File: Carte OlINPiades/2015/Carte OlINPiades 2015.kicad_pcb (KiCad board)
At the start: 2 copper layers, 283 parts, among them U1 dsPIC33FJ128MC802, U2 LM7805, U3 LM2937-3.3

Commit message: retourne leds
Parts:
- moved D1 1.00 mm to (47.5, 64.0), turned to 180 degrees
- moved D10 1.00 mm to (106.0, 64.0), turned to 180 degrees
- moved D100 1.00 mm to (67.0, 103.0), turned to 180 degrees
- moved D101 1.00 mm to (73.5, 103.0), turned to 180 degrees
- moved D102 1.00 mm to (80.0, 103.0), turned to 180 degrees
- moved D103 1.00 mm to (86.5, 103.0), turned to 180 degrees
- moved D104 1.00 mm to (93.0, 103.0), turned to 180 degrees
- moved D105 1.00 mm to (99.5, 103.0), turned to 180 degrees
- moved D106 1.00 mm to (106.0, 103.0), turned to 180 degrees
- moved D107 1.00 mm to (112.5, 103.0), turned to 180 degrees
- moved D108 1.00 mm to (119.0, 103.0), turned to 180 degrees
- moved D109 1.00 mm to (125.5, 103.0), turned to 180 degrees
- moved D11 1.00 mm to (112.5, 64.0), turned to 180 degrees
- moved D110 1.00 mm to (132.0, 103.0), turned to 180 degrees
- moved D111 1.00 mm to (138.5, 103.0), turned to 180 degrees
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
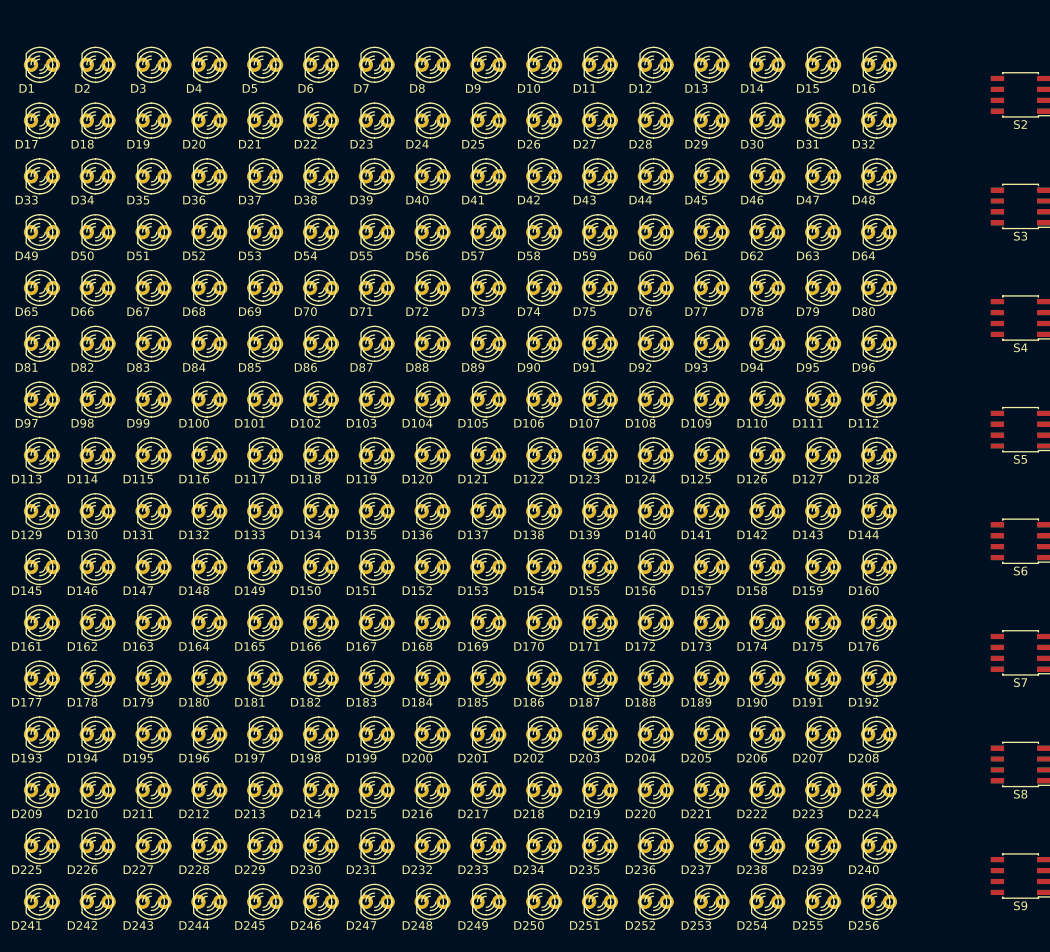
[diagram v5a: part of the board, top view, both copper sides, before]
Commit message: ajoute une face de piste de led
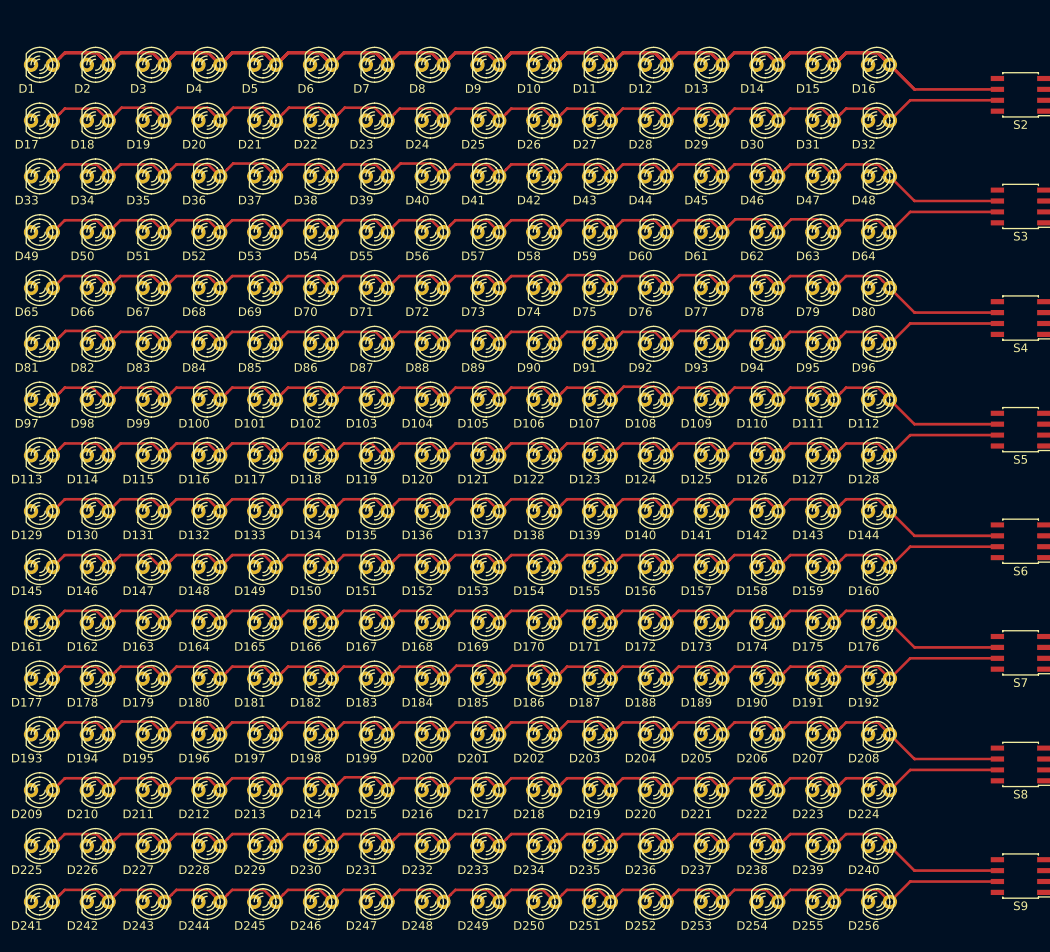
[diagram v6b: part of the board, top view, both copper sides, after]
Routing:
- net Net-(D1-Pad1): track 0.00 -> 477.0 mm
- net Net-(D17-Pad1): track 0.00 -> 128.8 mm
- net Net-(D65-Pad1): track 0.00 -> 128.7 mm
- net Net-(D193-Pad1): track 0.00 -> 128.7 mm
- net Net-(D33-Pad1): track 0.00 -> 128.7 mm
- net Net-(D81-Pad1): track 0.00 -> 128.7 mm
- net Net-(D100-Pad1): track 0.00 -> 128.6 mm
- net Net-(D225-Pad1): track 0.00 -> 128.5 mm
- net Net-(D161-Pad1): track 0.00 -> 128.5 mm
- net Net-(D129-Pad1): track 0.00 -> 128.5 mm
- net Net-(D49-Pad1): track 0.00 -> 128.5 mm
- net Net-(D177-Pad1): track 0.00 -> 128.5 mm
- net Net-(D209-Pad1): track 0.00 -> 128.4 mm
- net Net-(D241-Pad1): track 0.00 -> 128.3 mm
- net Net-(D145-Pad1): track 0.00 -> 128.3 mm
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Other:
- net class Pisa added: clearance 0.4, trace_width 0.308, via_dia 0.8, via_drill 0.6

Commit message: ajoute l'autre face de piste de leds
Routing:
- net Net-(D115-Pad2): track 0.00 -> 97.5 mm
- net Net-(D114-Pad2): track 0.00 -> 97.5 mm
- net Net-(D112-Pad2): track 0.00 -> 97.5 mm
- net Net-(D111-Pad2): track 0.00 -> 97.5 mm
- net Net-(D110-Pad2): track 0.00 -> 97.5 mm
- net Net-(D109-Pad2): track 0.00 -> 97.5 mm
- net Net-(D108-Pad2): track 0.00 -> 97.5 mm
- net Net-(D107-Pad2): track 0.00 -> 97.5 mm
- net Net-(D105-Pad2): track 0.00 -> 97.5 mm
- net Net-(D104-Pad2): track 0.00 -> 97.5 mm
- net Net-(D103-Pad2): track 0.00 -> 97.5 mm
- net Net-(D102-Pad2): track 0.00 -> 97.5 mm
- net Net-(D101-Pad2): track 0.00 -> 97.5 mm
- net Net-(D100-Pad2): track 0.00 -> 97.5 mm
- net Net-(D10-Pad2): track 0.00 -> 97.5 mm
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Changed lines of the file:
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@@
     (thickness 1.6)
     (drawings 0)
-    (tracks 1174)
+    (tracks 1191)
     (zones 0)
     (modules 283)
@@
   (segment (start 149.135 66.865) (end 146.27 64) (width 0.308) (layer F.Cu) (net 6))
   (segment (start 158.8 66.865) (end 149.135 66.865) (width 0.308) (layer F.Cu) (net 6))
+  (segment (start 46.23 64) (end 46.23 161.5) (width 0.308) (layer B.Cu) (net 7))
+  (segment (start 52.73 161.5) (end 52.73 64) (width 0.308) (layer B.Cu) (net 8))
+  (segment (start 59.23 64) (end 59.23 161.5) (width 0.308) (layer B.Cu) (net 9))
+  (segment (start 65.73 161.5) (end 65.73 64) (width 0.308) (layer B.Cu) (net 10))
+  (segment (start 72.23 64) (end 72.23 161.5) (width 0.308) (layer B.Cu) (net 11))
+  (segment (start 78.73 161.5) (end 78.73 64) (width 0.308) (layer B.Cu) (net 12))
+  (segment (start 85.23 64) (end 85.23 161.5) (width 0.308) (layer B.Cu) (net 13))
+  (segment (start 91.73 161.5) (end 91.73 64) (width 0.308) (layer B.Cu) (net 14))
+  (segment (start 98.23 64) (end 98.23 161.5) (width 0.308) (layer B.Cu) (net 15))
+  (segment (start 104.73 161.5) (end 104.73 64) (width 0.308) (layer B.Cu) (net 16))
+  (segment (start 111.23 64) (end 111.23 161.5) (width 0.308) (layer B.Cu) (net 17))
+  (segment (start 117.73 161.5) (end 117.73 64) (width 0.308) (layer B.Cu) (net 18))
+  (segment (start 124.23 64) (end 124.23 161.5) (width 0.308) (layer B.Cu) (net 19))
+  (segment (start 130.73 161.5) (end 130.73 64) (width 0.308) (layer B.Cu) (net 20))
+  (segment (start 137.23 64) (end 137.23 148.020458) (width 0.308) (layer B.Cu) (net 21))
+  (segment (start 137.23 148.020458) (end 137.23 161.5) (width 0.308) (layer B.Cu) (net 21))
+  (segment (start 143.73 161.5) (end 143.73 64) (width 0.308) (layer B.Cu) (net 22))
   (segment (start 55.27 70.5) (end 53.877799 69.107799) (width 0.308) (layer F.Cu) (net 23))
   (segment (start 53.877799 69.107799) (end 50.162201 69.107799) (width 0.308) (layer F.Cu) (net 23))

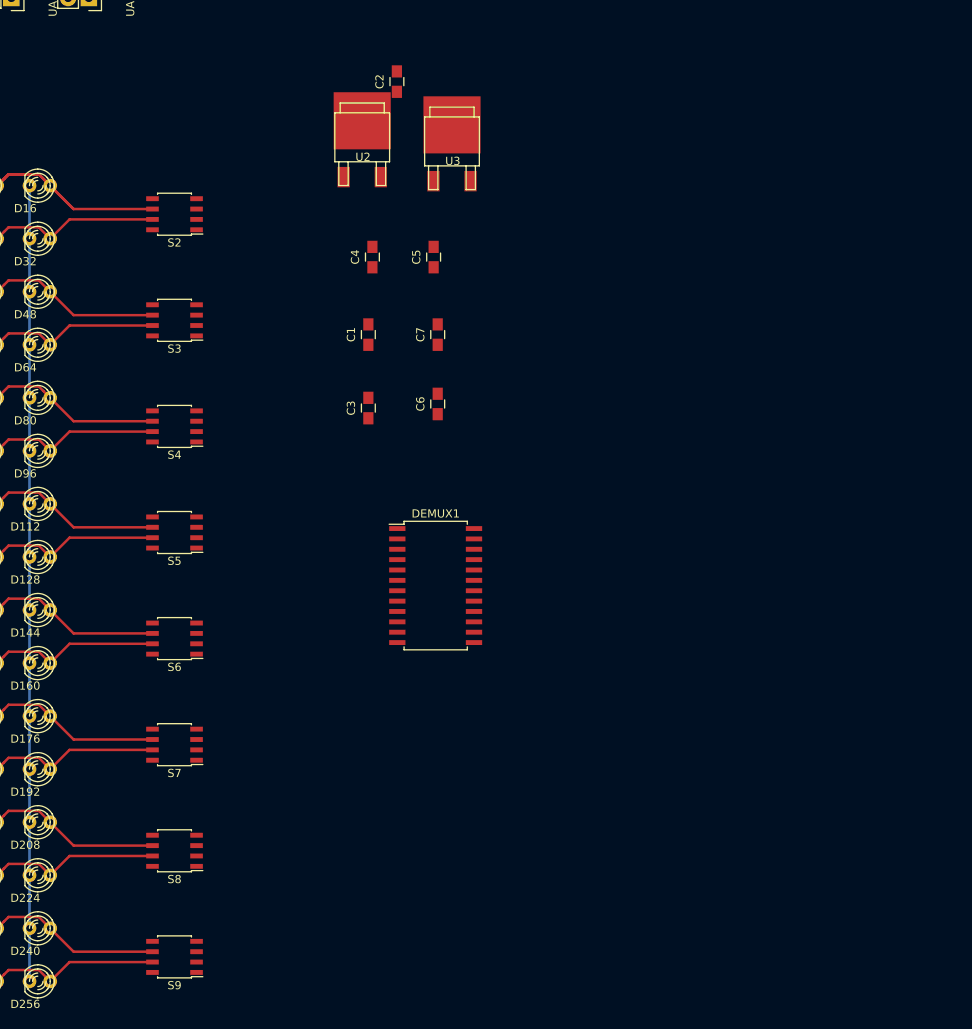
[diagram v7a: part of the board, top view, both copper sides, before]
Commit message: ajoute pistes coté demux
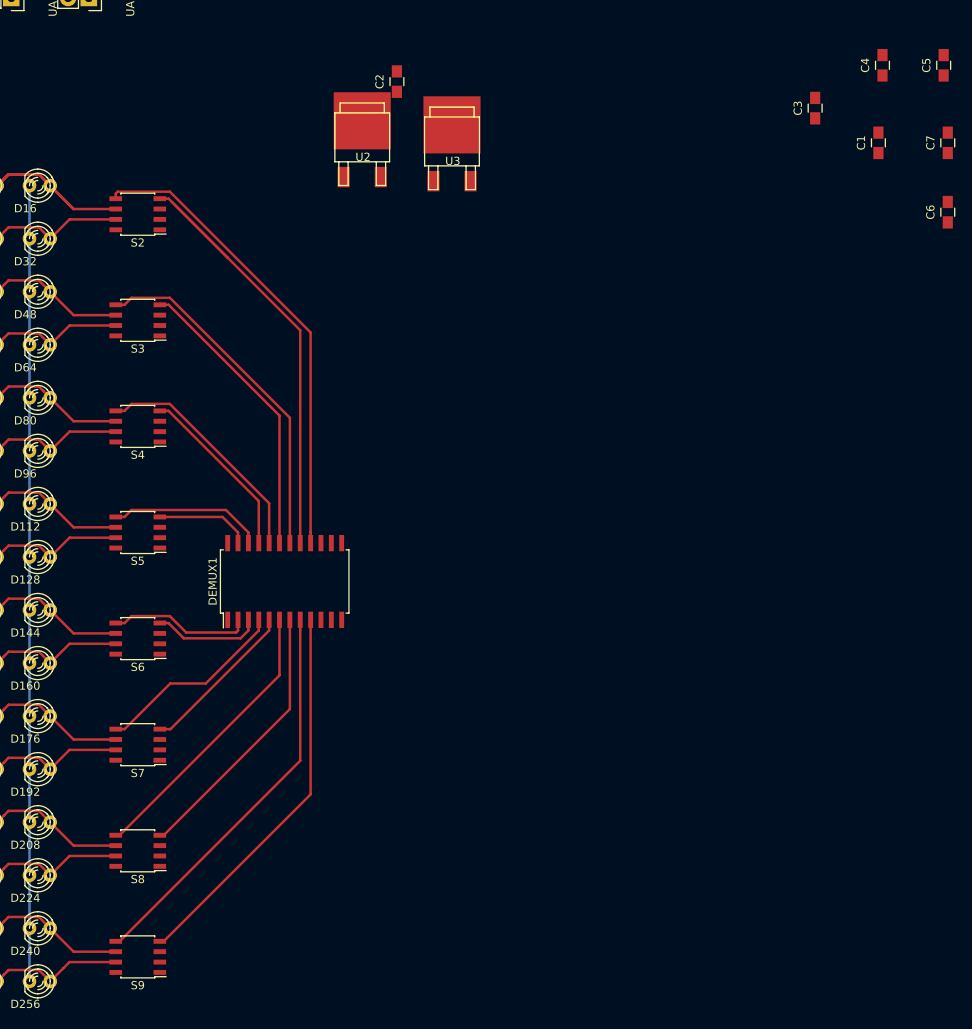
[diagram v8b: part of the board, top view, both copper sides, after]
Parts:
- moved C1 66.8 mm to (247.8, 58.8)
- moved C4 66.8 mm to (248.2, 49.2)
- moved C5 66.8 mm to (255.8, 49.2)
- moved C6 66.8 mm to (256.2, 67.2)
- moved C7 66.8 mm to (256.2, 58.8)
- moved C3 65.9 mm to (240.0, 54.5)
- moved DEMUX1 18.5 mm to (175.0, 112.5), turned to 90 degrees
- moved S2 4.50 mm to (157.0, 67.5)
- moved S3 4.50 mm to (157.0, 80.5)
- moved S4 4.50 mm to (157.0, 93.5)
- moved S5 4.50 mm to (157.0, 106.5)
- moved S6 4.50 mm to (157.0, 119.5)
- moved S7 4.50 mm to (157.0, 132.5)
- moved S8 4.50 mm to (157.0, 145.5)
- moved S9 4.50 mm to (157.0, 158.5)
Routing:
- net Net-(DEMUX1-Pad17): track 0.00 -> 59.6 mm
- net Net-(DEMUX1-Pad16): track 0.00 -> 57.5 mm
- net Net-(DEMUX1-Pad8): track 0.00 -> 49.0 mm
- net Net-(DEMUX1-Pad9): track 0.00 -> 47.3 mm
- net Net-(DEMUX1-Pad18): track 0.00 -> 43.1 mm
- net Net-(DEMUX1-Pad19): track 0.00 -> 35.9 mm
- net Net-(DEMUX1-Pad6): track 0.00 -> 35.0 mm
- net Net-(DEMUX1-Pad7): track 0.00 -> 33.3 mm
- net Net-(DEMUX1-Pad20): track 0.00 -> 29.1 mm
- net Net-(DEMUX1-Pad4): track 0.00 -> 23.8 mm
- net Net-(DEMUX1-Pad21): track 0.00 -> 21.9 mm
- net Net-(DEMUX1-Pad5): track 0.00 -> 19.7 mm
- net Net-(DEMUX1-Pad22): track 0.00 -> 19.1 mm
- net Net-(DEMUX1-Pad2): track 0.00 -> 17.6 mm
- net Net-(DEMUX1-Pad3): track 0.00 -> 13.3 mm
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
